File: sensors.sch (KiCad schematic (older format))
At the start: 13 parts, among them U10 HMC5883L, U11 H3LIS331DL, U8 MS5611-01BA, U9 MPU6000

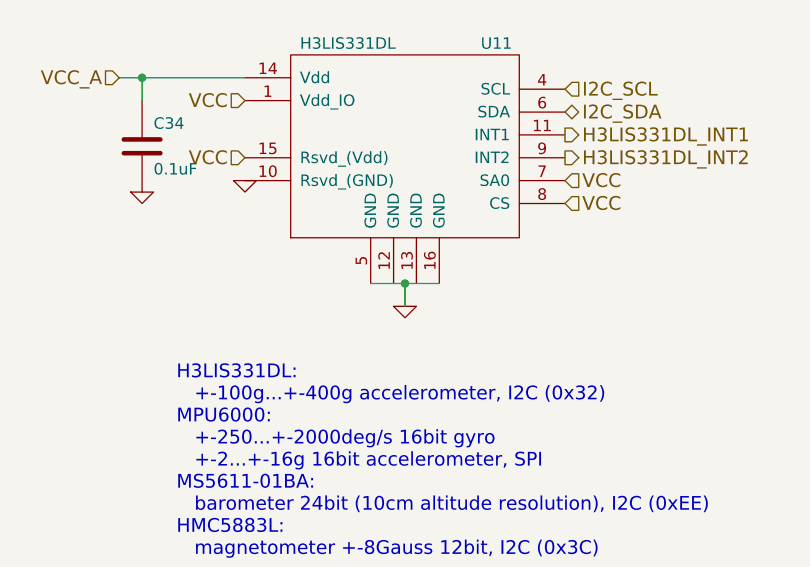
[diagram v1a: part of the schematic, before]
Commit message: fix errors detected by ERC
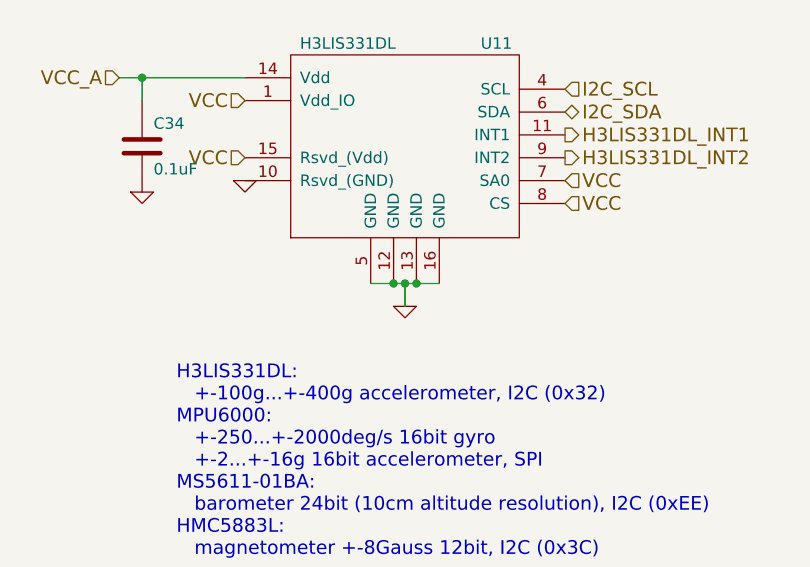
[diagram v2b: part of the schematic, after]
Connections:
- net GND: now also U11.12 (GND), U11.13 (GND)
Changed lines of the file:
@@
 $EndComp
 $Comp
-L GND #PWR057
+L GND #PWR058
 U 1 1 518B161E
 P 2450 4250
-F 0 "#PWR057" H 2450 4250 30  0001 C CNN
+F 0 "#PWR058" H 2450 4250 30  0001 C CNN
 F 1 "GND" H 2450 4180 30  0001 C CNN
 F 2 "" H 2450 4250 60  0001 C CNN
@@
 $EndComp
 $Comp
-L GND #PWR058
+L GND #PWR059
 U 1 1 518B161C
 P 1400 4550
-F 0 "#PWR058" H 1400 4550 30  0001 C CNN
+F 0 "#PWR059" H 1400 4550 30  0001 C CNN
 F 1 "GND" H 1400 4480 30  0001 C CNN
 F 2 "" H 1400 4550 60  0001 C CNN
@@
 $EndComp
 $Comp
-L GND #PWR059
+L GND #PWR060
 U 1 1 518B161B
 P 2100 4950
-F 0 "#PWR059" H 2100 4950 30  0001 C CNN
+F 0 "#PWR060" H 2100 4950 30  0001 C CNN
 F 1 "GND" H 2100 4880 30  0001 C CNN
 F 2 "" H 2100 4950 60  0001 C CNN
@@
 $EndComp
 $Comp
-L GND #PWR060
+L GND #PWR061
 U 1 1 518B1619
 P 2450 5050
-F 0 "#PWR060" H 2450 5050 30  0001 C CNN
+F 0 "#PWR061" H 2450 5050 30  0001 C CNN
 F 1 "GND" H 2450 4980 30  0001 C CNN
 F 2 "" H 2450 5050 60  0001 C CNN
@@
 $EndComp
 $Comp
-L GND #PWR061
+L GND #PWR062
 U 1 1 518B1613
 P 7250 2200
-F 0 "#PWR061" H 7250 2200 30  0001 C CNN
+F 0 "#PWR062" H 7250 2200 30  0001 C CNN
 F 1 "GND" H 7250 2130 30  0001 C CNN
 F 2 "" H 7250 2200 60  0001 C CNN
@@
 $EndComp
 $Comp
-L GND #PWR062
+L GND #PWR063
 U 1 1 518B1610
 P 8800 2600
-F 0 "#PWR062" H 8800 2600 30  0001 C CNN
+F 0 "#PWR063" H 8800 2600 30  0001 C CNN
 F 1 "GND" H 8800 2530 30  0001 C CNN
 F 2 "" H 8800 2600 60  0001 C CNN
@@
 NoConn ~ 3900 1850
 $Comp
-L GND #PWR063
+L GND #PWR064
 U 1 1 518B160E
 P 3900 2100
-F 0 "#PWR063" H 3900 2100 30  0001 C CNN
+F 0 "#PWR064" H 3900 2100 30  0001 C CNN
 F 1 "GND" H 3900 2030 30  0001 C CNN
 F 2 "" H 3900 2100 60  0001 C CNN
@@
 $EndComp
 $Comp
-L GND #PWR064
+L GND #PWR065
 U 1 1 518B160D
 P 2300 2150
-F 0 "#PWR064" H 2300 2150 30  0001 C CNN
+F 0 "#PWR065" H 2300 2150 30  0001 C CNN
 F 1 "GND" H 2300 2080 30  0001 C CNN
 F 2 "" H 2300 2150 60  0001 C CNN
@@
 Connection ~ 7250 4250
 $Comp
-L GND #PWR065
+L GND #PWR066
 U 1 1 5196E087
 P 7250 4750
-F 0 "#PWR065" H 7250 4750 30  0001 C CNN
+F 0 "#PWR066" H 7250 4750 30  0001 C CNN
 F 1 "GND" H 7250 4680 30  0001 C CNN
 F 2 "" H 7250 4750 60  0000 C CNN
@@
 $EndComp
 $Comp
-L GND #PWR066
+L GND #PWR067
 U 1 1 5196E096
 P 8400 5250
-F 0 "#PWR066" H 8400 5250 30  0001 C CNN
+F 0 "#PWR067" H 8400 5250 30  0001 C CNN
 F 1 "GND" H 8400 5180 30  0001 C CNN
 F 2 "" H 8400 5250 60  0000 C CNN
@@
 Connection ~ 8400 5150
 $Comp
-L GND #PWR067
+L GND #PWR068
 U 1 1 5196E151
 P 7700 4700
-F 0 "#PWR067" H 7700 4700 30  0001 C CNN
+F 0 "#PWR068" H 7700 4700 30  0001 C CNN
 F 1 "GND" H 7700 4630 30  0001 C CNN
 F 2 "" H 7700 4700 60  0000 C CNN
@@
 Text HLabel 9100 4600 2    60   Output ~ 0
 H3LIS331DL_INT2
+Connection ~ 8350 5150
+Connection ~ 8450 5150
 $EndSCHEMATC

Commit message: switched to renamed component and footprint libraries
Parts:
- U10: symbol HMC5883L -> _HMC5883L
- U11: symbol H3LIS331DL -> _H3LIS331DL
- U8: symbol MS5611-01BA -> _MS5611-01BA
- U9: symbol MPU6000 -> _MPU6000
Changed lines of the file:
@@
 LIBS:contrib
 LIBS:valves
-LIBS:connectors
-LIBS:div
-LIBS:sensors
-LIBS:stm32
-LIBS:linear-regulators
+LIBS:_connectors
+LIBS:_div
+LIBS:_sensors
+LIBS:_stm32
+LIBS:_linear-regulators
 LIBS:ins-board-cache
 EELAYER 27 0
@@
 VCC
 $Comp
-L MPU6000 U9
+L _MPU6000 U9
 U 1 1 518B161F
 P 3600 4550
@@
 NoConn ~ 2650 4900
 $Comp
-L HMC5883L U10
+L _HMC5883L U10
 U 1 1 518B1617
 P 8250 1800
@@
 $EndComp
 $Comp
-L MS5611-01BA U8
+L _MS5611-01BA U8
 U 1 1 518B160F
 P 3150 1850
@@
 $EndComp
 $Comp
-L H3LIS331DL U11
+L _H3LIS331DL U11
 U 1 1 5196DFD7
 P 8400 4600

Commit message: updated some capacitor footprints
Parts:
- added C37: 10uF, ~, symbol C
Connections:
- wire segments 30 -> 33
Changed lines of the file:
@@
 LIBS:_linear-regulators
 LIBS:ins-board-cache
-EELAYER 24 0
+EELAYER 27 0
 EELAYER END
 $Descr A4 11693 8268
@@
 Sheet 2 2
 Title "Sensors"
-Date "9 feb 2014"
+Date "11 feb 2014"
 Rev ""
 Comp ""
@@
 $EndComp
 $Comp
-L GND #PWR58
+L GND #PWR055
 U 1 1 518B161E
 P 2450 4250
-F 0 "#PWR58" H 2450 4250 30  0001 C CNN
+F 0 "#PWR055" H 2450 4250 30  0001 C CNN
 F 1 "GND" H 2450 4180 30  0001 C CNN
 F 2 "" H 2450 4250 60  0001 C CNN
@@
 $EndComp
 $Comp
-L GND #PWR55
+L GND #PWR056
 U 1 1 518B161C
 P 1400 4550
-F 0 "#PWR55" H 1400 4550 30  0001 C CNN
+F 0 "#PWR056" H 1400 4550 30  0001 C CNN
 F 1 "GND" H 1400 4480 30  0001 C CNN
 F 2 "" H 1400 4550 60  0001 C CNN
@@
 $EndComp
 $Comp
-L GND #PWR56
+L GND #PWR057
 U 1 1 518B161B
 P 2100 4950
-F 0 "#PWR56" H 2100 4950 30  0001 C CNN
+F 0 "#PWR057" H 2100 4950 30  0001 C CNN
 F 1 "GND" H 2100 4880 30  0001 C CNN
 F 2 "" H 2100 4950 60  0001 C CNN
@@
 $EndComp
 $Comp
-L GND #PWR59
+L GND #PWR058
 U 1 1 518B1619
 P 2450 5050
-F 0 "#PWR59" H 2450 5050 30  0001 C CNN
+F 0 "#PWR058" H 2450 5050 30  0001 C CNN
 F 1 "GND" H 2450 4980 30  0001 C CNN
 F 2 "" H 2450 5050 60  0001 C CNN
@@
 $EndComp
 $Comp
-L GND #PWR61
+L GND #PWR059
 U 1 1 518B1613
 P 7250 2200
-F 0 "#PWR61" H 7250 2200 30  0001 C CNN
+F 0 "#PWR059" H 7250 2200 30  0001 C CNN
 F 1 "GND" H 7250 2130 30  0001 C CNN
 F 2 "" H 7250 2200 60  0001 C CNN
@@
 $EndComp
 $Comp
-L GND #PWR65
+L GND #PWR060
 U 1 1 518B1610
 P 8800 2600
-F 0 "#PWR65" H 8800 2600 30  0001 C CNN
+F 0 "#PWR060" H 8800 2600 30  0001 C CNN
 F 1 "GND" H 8800 2530 30  0001 C CNN
 F 2 "" H 8800 2600 60  0001 C CNN
@@
 NoConn ~ 3900 1850
 $Comp
-L GND #PWR60
+L GND #PWR061
 U 1 1 518B160E
 P 3900 2100
-F 0 "#PWR60" H 3900 2100 30  0001 C CNN
+F 0 "#PWR061" H 3900 2100 30  0001 C CNN
 F 1 "GND" H 3900 2030 30  0001 C CNN
 F 2 "" H 3900 2100 60  0001 C CNN
@@
 $EndComp
 $Comp
-L GND #PWR57
+L GND #PWR062
 U 1 1 518B160D
 P 2300 2150
-F 0 "#PWR57" H 2300 2150 30  0001 C CNN
+F 0 "#PWR062" H 2300 2150 30  0001 C CNN
 F 1 "GND" H 2300 2080 30  0001 C CNN
 F 2 "" H 2300 2150 60  0001 C CNN
@@
 Connection ~ 7250 4250
 $Comp
-L GND #PWR62
+L GND #PWR063
 U 1 1 5196E087
-P 7250 4750
-F 0 "#PWR62" H 7250 4750 30  0001 C CNN
-F 1 "GND" H 7250 4680 30  0001 C CNN
-F 2 "" H 7250 4750 60  0000 C CNN
-F 3 "" H 7250 4750 60  0000 C CNN
-	1    7250 4750
-	1    0    0    -1
-$EndComp
-$Comp
-L GND #PWR64
+P 7150 4800
+F 0 "#PWR063" H 7150 4800 30  0001 C CNN
+F 1 "GND" H 7150 4730 30  0001 C CNN
+F 2 "" H 7150 4800 60  0000 C CNN
+F 3 "" H 7150 4800 60  0000 C CNN
+	1    7150 4800
+	1    0    0    -1
+$EndComp
+$Comp
+L GND #PWR064
 U 1 1 5196E096
 P 8400 5250
-F 0 "#PWR64" H 8400 5250 30  0001 C CNN
+F 0 "#PWR064" H 8400 5250 30  0001 C CNN
 F 1 "GND" H 8400 5180 30  0001 C CNN
 F 2 "" H 8400 5250 60  0000 C CNN
@@
 Connection ~ 8400 5150
 $Comp
-L GND #PWR63
+L GND #PWR065
 U 1 1 5196E151
 P 7700 4700
-F 0 "#PWR63" H 7700 4700 30  0001 C CNN
+F 0 "#PWR065" H 7700 4700 30  0001 C CNN
 F 1 "GND" H 7700 4630 30  0001 C CNN
 F 2 "" H 7700 4700 60  0000 C CNN
@@
 Connection ~ 8350 5150
 Connection ~ 8450 5150
+$Comp
+L C C37
+U 1 1 52FA56B3
+P 7000 4550
+F 0 "C37" H 7000 4650 40  0000 L CNN
+F 1 "10uF" H 7006 4465 40  0000 L CNN
+F 2 "~" H 7038 4400 30  0000 C CNN
+F 3 "~" H 7000 4550 60  0000 C CNN
+	1    7000 4550
+	1    0    0    -1
+$EndComp
+Wire Wire Line
+	7000 4750 7250 4750
+Wire Wire Line
+	7000 4350 7250 4350
+Connection ~ 7250 4350
+Connection ~ 7250 4750
+Wire Wire Line
+	7150 4750 7150 4800
+Connection ~ 7150 4750
 $EndSCHEMATC
